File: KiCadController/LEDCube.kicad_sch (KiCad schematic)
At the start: 56 parts, among them IC100 MCP73833T-FCI_MF, IC101 CP2102N-A02-GQFN28, IC102 ESP32-WROOM-32E-H4, J100 1769, J102 USB4110-GF-A, J103 15-91-0100, J104 15-91-0100, J105 15-91-0100, J106 15-91-0100, J107 15-91-0100, J108 15-91-0100, Q100 Q_NMOS_GSD, Q101 Q_NMOS_GSD, Q102 Q_NMOS_GSD, Q103 Q_NMOS_GSD, Q104 Q_NMOS_GSD

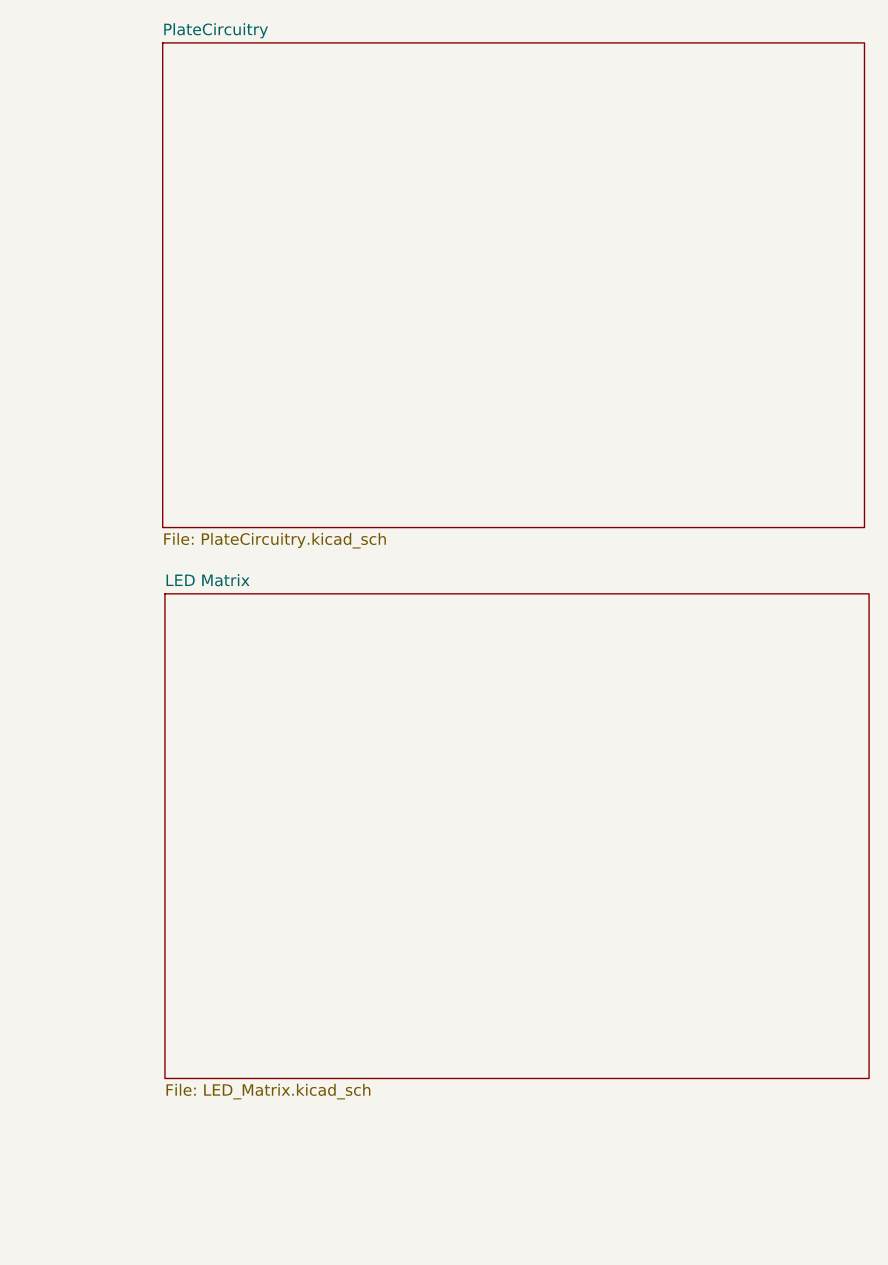
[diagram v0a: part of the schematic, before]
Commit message: [PCB] Split schematic into two board for easier routing
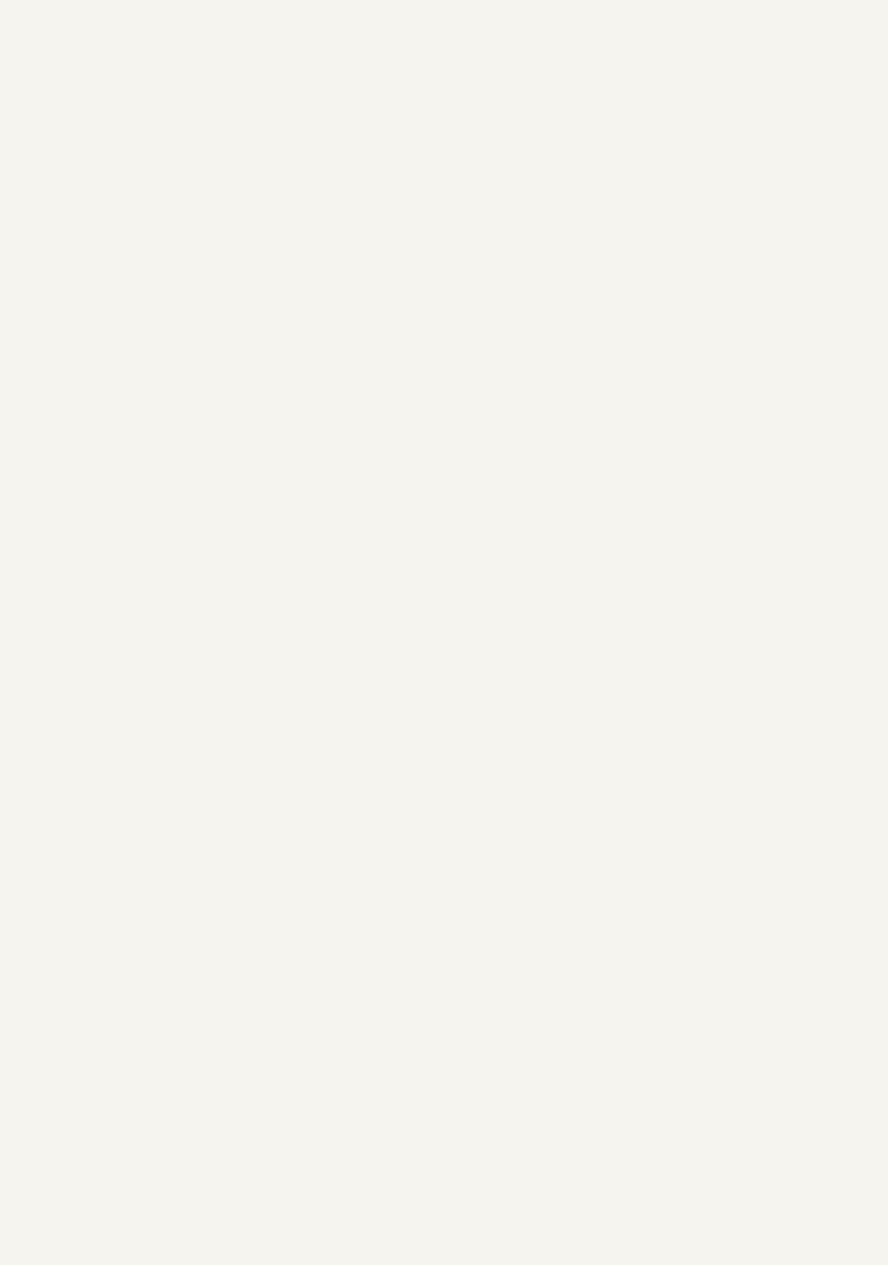
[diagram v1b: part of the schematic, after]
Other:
- removed sheet LED Matrix
- removed sheet PlateCircuitry
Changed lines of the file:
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@@
-    )
-  )
-  (sheet (at 421.894 72.136) (size 78.232 53.848) (fields_autoplaced)
-    (stroke (width 0.1524) (type solid))
-    (fill (color 0 0 0 0.0000))
-    (property "Sheetname" "LED Matrix" (at 421.894 71.4244 0)
-      (effects (font (size 1.27 1.27)) (justify left bottom))
-    )
-    (property "Sheetfile" "LED_Matrix.kicad_sch" (at 421.894 126.5686 0)
-      (effects (font (size 1.27 1.27)) (justify left top))
-    )
-    (instances
-      (project "LEDCube"
-        (path "/9a63682e-9260-46ec-acb0-b5bfe37f690e" (page "3"))
-      )
-    )
-  )
-  (sheet (at 421.64 10.922) (size 77.978 53.848) (fields_autoplaced)
-    (stroke (width 0.1524) (type solid))
-    (fill (color 0 0 0 0.0000))
-    (property "Sheetname" "PlateCircuitry" (at 421.64 10.2104 0)
-      (effects (font (size 1.27 1.27)) (justify left bottom))
-    )
-    (property "Sheetfile" "PlateCircuitry.kicad_sch" (at 421.64 65.3546 0)
-      (effects (font (size 1.27 1.27)) (justify left top))
-    )
-    (instances
-      (project "LEDCube"
-        (path "/9a63682e-9260-46ec-acb0-b5bfe37f690e" (page "2"))
-      )
     )
   )

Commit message: Update for MTE
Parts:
- removed Q100, Q101, Q102: Q_NMOS_GSD, SamacSys_Parts:SOT96P237X111-3N, symbol Device:Q_NMOS_GSD
- removed R104: 3.3k, Resistor_SMD:R_0603_1608Metric, symbol Device:R
- removed R105, R117: 10k, Resistor_SMD:R_0603_1608Metric, symbol Device:R
- removed R106: 2.49k, Resistor_SMD:R_0603_1608Metric, symbol Device:R
- added H100, H101, H102, H103: MountingHole, MountingHole:MountingHole_3.2mm_M3_Pad_Via, symbol Mechanical:MountingHole
- added R111: 2k, Resistor_SMD:R_0603_1608Metric, symbol Device:R
- IC102: footprint ESP32WROOM32EH4 -> SamacSys_Parts:ESP32WROOM32EH4
- J103: renamed from J106; footprint SamacSys_Parts:FTSH10501FDVK -> LEDCube:CNC_TECH_SMD_10POS
- J104: renamed from J103; footprint SamacSys_Parts:FTSH10501FDVK -> LEDCube:CNC_TECH_SMD_10POS
- J105: renamed from J108; footprint SamacSys_Parts:FTSH10501FDVK -> LEDCube:CNC_TECH_SMD_10POS
- J106: renamed from J105; footprint SamacSys_Parts:FTSH10501FDVK -> LEDCube:CNC_TECH_SMD_10POS
- J107: footprint SamacSys_Parts:FTSH10501FDVK -> LEDCube:CNC_TECH_SMD_10POS
- J108: renamed from J104; footprint SamacSys_Parts:FTSH10501FDVK -> LEDCube:CNC_TECH_SMD_10POS
- renumbered C105 to C102, C106 to C103, C110 to C104, C102 to C105, C107 to C106, C108 to C107, C109 to C108, C103 to C109, C104 to C110, IC101 to IC100, IC100 to IC101, J102 to J100, J100 to J102, Q103 to Q100, Q104 to Q101, R108 to R100, R109 to R101, R103 to R102, R120 to R103, R121 to R104, R100 to R105, R112 to R106, R101 to R107, R102 to R108, R107 to R109, R113 to R110, R115 to R112, R118 to R113, R116 to R114, R119 to R115, R110 to R116, R111 to R117, R114 to R119, U101 to U100, U100 to U101
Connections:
- net BRIGHTNESS_PWM: now also IC102.37 (IO23); no longer IC102.28 (IO17)
- net EN: now also C111.1, IC102.3 (EN), R119.2
- net GND: now also R111.2
- net LATCH: now also IC102.30 (IO18); no longer IC102.33 (IO21)
- net MASTER_CLK: now also IC102.33 (IO21); no longer IC102.36 (IO22)
- net MUX_B0: now also IC102.36 (IO22); no longer IC102.30 (IO18)
- net MUX_B3: now also IC102.28 (IO17); no longer IC102.27 (IO16)
- net SERIAL_IN0: now also IC102.27 (IO16); no longer IC102.37 (IO23)
- net at IC101.6 (PROG): now also R111.1
- net CHG_1.5A: no longer names the net of IC100.14 (CHR1)
- net CHG_100mA: no longer names the net of IC100.13 (CHREN)
- net CHG_100mA: no longer IC102.5 (SENSOR_VN)
- net CHG_500mA: no longer names the net of IC100.15 (CHR0)
- no-connect marks 33 -> 37
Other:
- note added: "Mouting Holes to Panel"
- note added: "PROG at 2k -> 500mA fast charge. Reasonable to assume all wall warts will support."
- note removed: "USB 100mA, just 10k -> 100mA USB 500mA, 10k | 2.49k = 1993 -> 500mA USB >500mA, 10k | 2.49k | 3.3k = 1243 -> 800mA (conservative battery maximum)"
